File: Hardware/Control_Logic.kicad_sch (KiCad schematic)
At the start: 19 parts, among them IC18 74HC139, IC25 74HC138, IC27 74HC32, IC28 74HC00, IC29 74AHC04, IC30 74HC02, IC31 74HC273, IC32 74HC138, IC49 74HC367, J101 CS Test Points, J7 Decoder

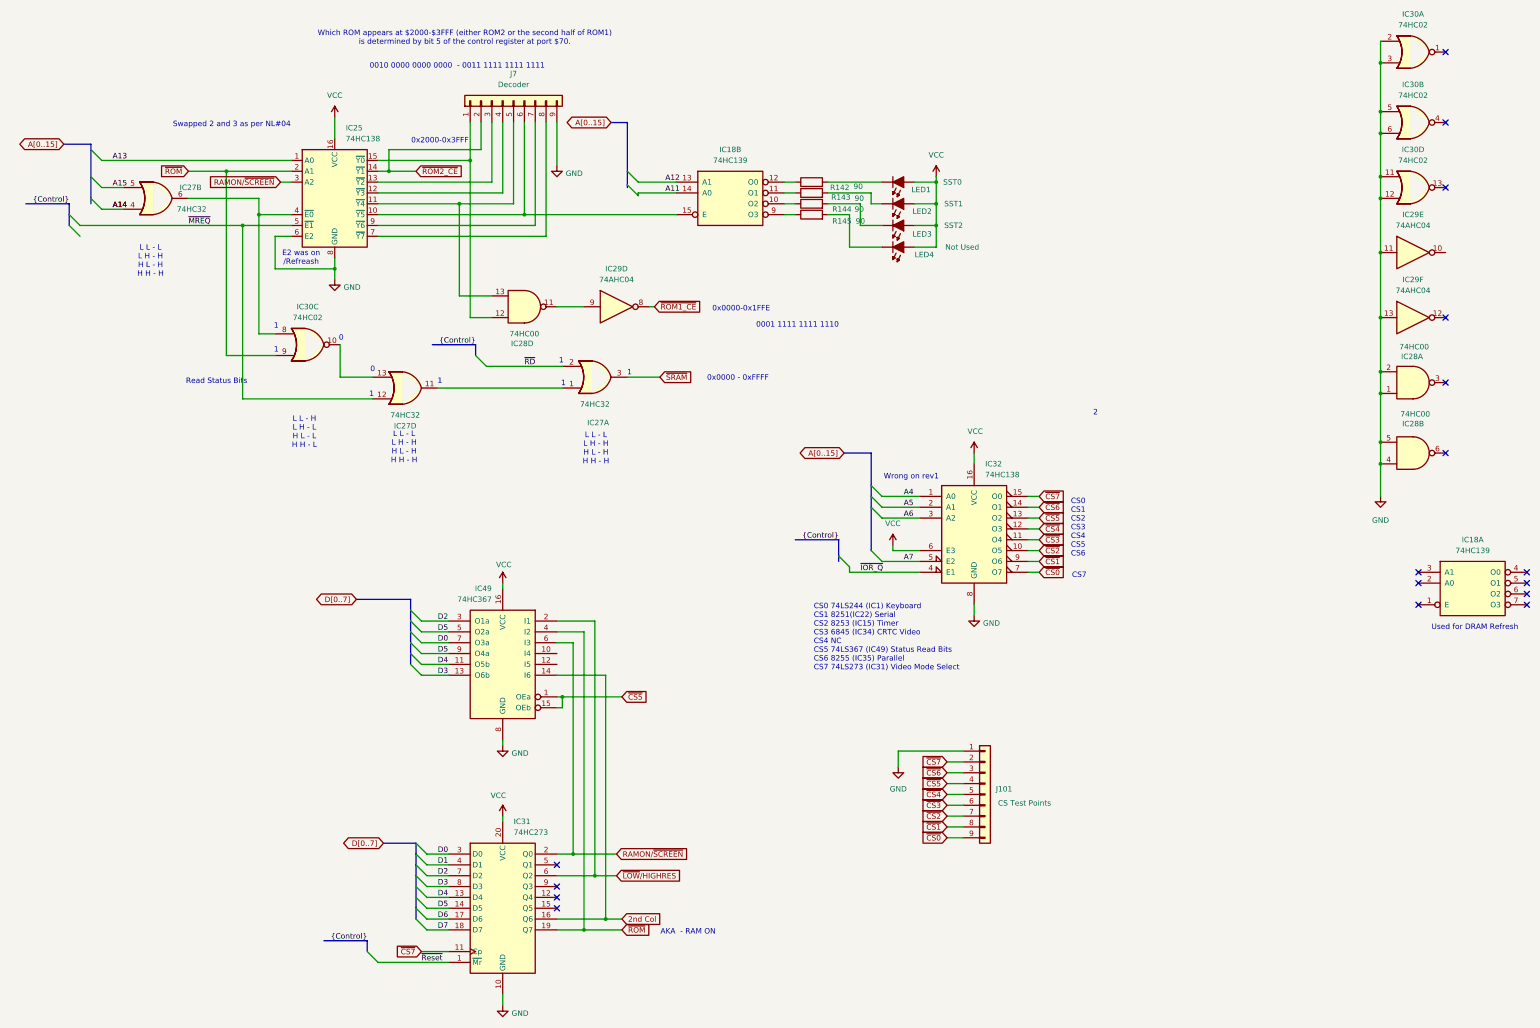
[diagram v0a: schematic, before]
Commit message: Fixed some issues with memory mapping IC 25
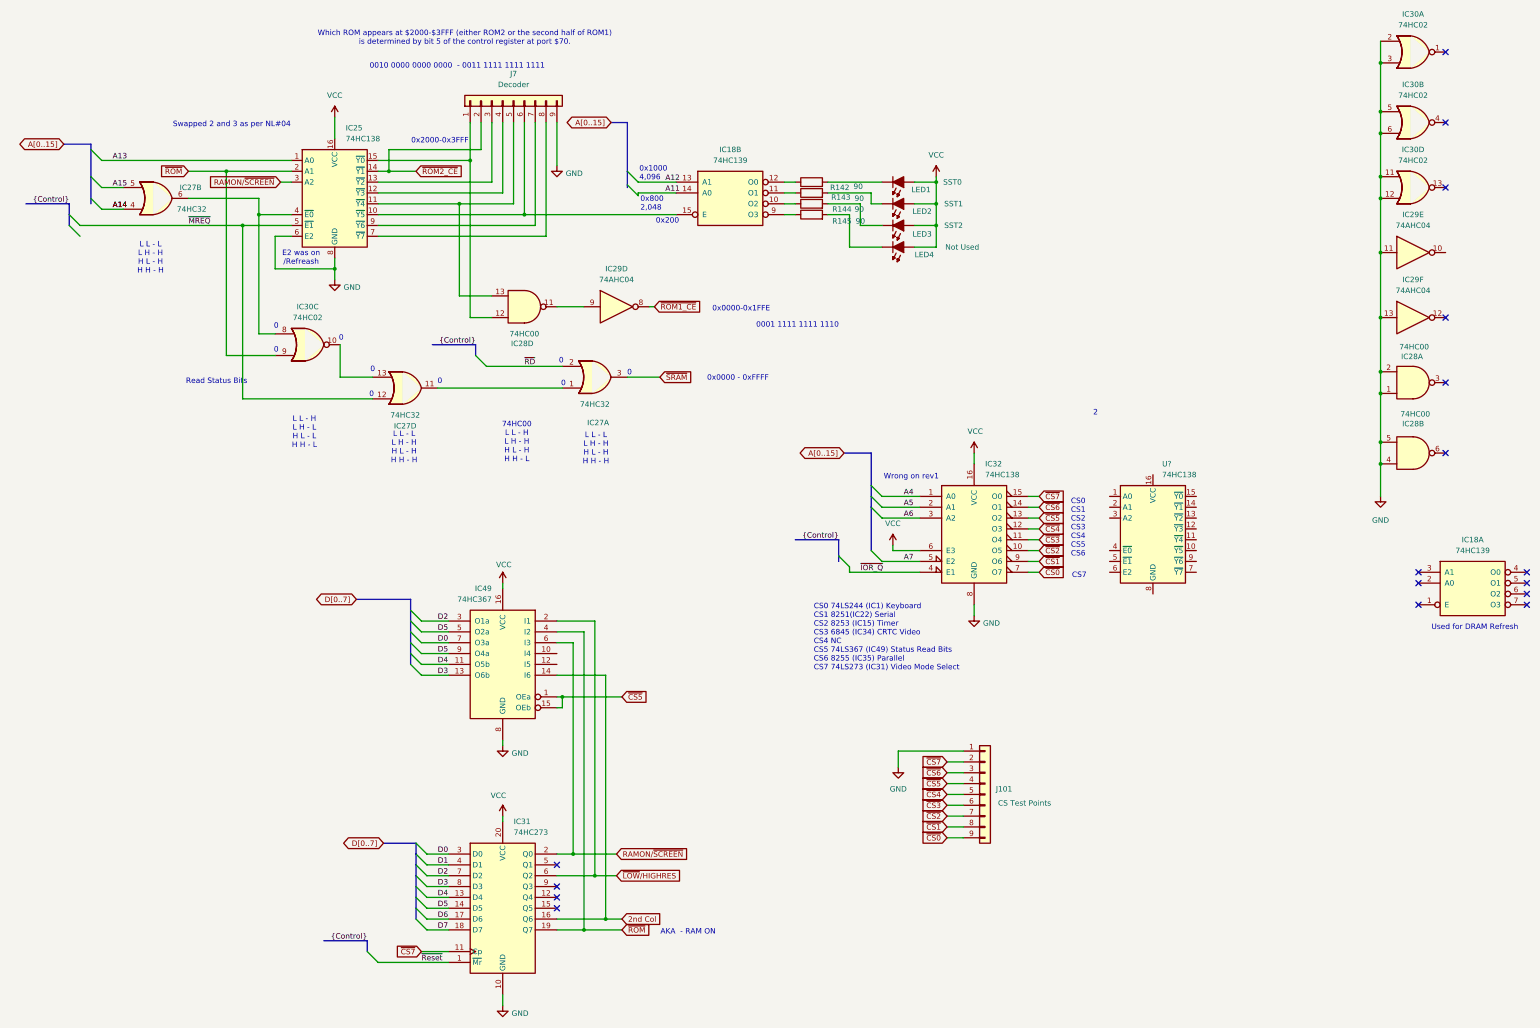
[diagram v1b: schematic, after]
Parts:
- added U?: 74HC138, Package_DIP:DIP-16_W7.62mm_Socket_LongPads, symbol 74xx:74HC138
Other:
- note added: "0x1000 4,096"
- note added: "0x200"
- note added: "0x800 2,048"
- note added: "74HC00 L L - H L H - H H L - H H H - L"
- note removed: "1"
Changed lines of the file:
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@@
 		)
 	)
-	(text "1"
+	(text "0"
 		(exclude_from_sim no)
 		(at 135.128 106.426 0)
@@
 		)
 	)
-	(text "1"
+	(text "0"
 		(exclude_from_sim no)
 		(at 119.126 109.474 0)
@@
 	(text "L L - L\nL H - H\nH L - H\nH H - H"
 		(exclude_from_sim no)
-		(at 67.31 78.232 0)
+		(at 67.31 77.47 0)
 		(effects
 			(font
@@
 		)
 	)
+	(text "0x1000\n4,096"
+		(exclude_from_sim no)
+		(at 181.864 57.658 0)
+		(effects
+			(font
+				(size 1.27 1.27)
+			)
+			(justify left)
+		)
+	)
 	(text "Used for DRAM Refresh"
 		(exclude_from_sim no)
@@
 		)
 	)
+	(text "0x200"
+		(exclude_from_sim no)
+		(at 188.468 68.834 0)
+		(effects
+			(font
+				(size 1.27 1.27)
+			)
+		)
+	)
 	(text "E2 was on \n/Refreash"
 		(exclude_from_sim no)
@@
 		)
 	)
+	(text "0x800 \n2,048"
+		(exclude_from_sim no)
+		(at 182.118 64.77 0)
+		(effects
+			(font
+				(size 1.27 1.27)
+			)
+			(justify left)
+		)
+	)
 	(text "CS0 74LS244 (IC1) Keyboard\nCS1 8251(IC22) Serial\nCS2 8253 (IC15) Timer\nCS3 6845 (IC34) CRTC Video\nCS4 NC\nCS5 74LS367 (IC49) Status Read Bits\nCS6 8255 (IC35) Parallel \nCS7 74LS273 (IC31) Video Mode Select"
 		(exclude_from_sim no)
@@
 		)
 	)
-	(text "1"
+	(text "0"
 		(exclude_from_sim no)
 		(at 164.084 106.934 0)
@@
 		)
 	)
-	(text "1"
+	(text "0"
 		(exclude_from_sim no)
 		(at 163.576 101.6 0)
@@
 		)
 	)
-	(text "1"
+	(text "0"
 		(exclude_from_sim no)
 		(at 179.578 104.394 0)
@@
 		)
 	)
-	(text "1"
+	(text "0"
 		(exclude_from_sim no)
 		(at 96.774 93.472 0)
@@
 		)
 	)
-	(text "1"
+	(text "0"
 		(exclude_from_sim no)
 		(at 96.774 99.06 0)
@@
 		)
 	)
+	(text "74HC00\nL L - H\nL H - H\nH L - H\nH H - L"
+		(exclude_from_sim no)
+		(at 153.162 120.65 0)
+		(effects
+			(font
+				(size 1.27 1.27)
+			)
+		)
+	)
 	(text "0x2000-0x3FFF"
 		(exclude_from_sim no)
@@
 	)
 	(junction
-		(at 88.9 69.85)
+		(at 355.6 63.5)
 		(diameter 0)
 		(color 0 0 0 0)
 	)
 	(junction
-		(at 355.6 63.5)
+		(at 355.6 104.14)
 		(diameter 0)
 		(color 0 0 0 0)
 	)
 	(junction
-		(at 355.6 104.14)
+		(at 139.7 64.77)
 		(diameter 0)
 		(color 0 0 0 0)
 	)
 	(junction
-		(at 139.7 64.77)
+		(at 88.9 69.85)
 		(diameter 0)
 		(color 0 0 0 0)
@@
 	)
 	(bus_entry
+		(at 48.26 67.31)
+		(size 2.54 2.54)
+		(stroke
+			(width 0)
+			(type default)
+		)
+	)
+	(bus_entry
 		(at 53.34 52.07)
 		(size 2.54 2.54)
@@
 	)
 	(bus_entry
-		(at 48.26 67.31)
-		(size 2.54 2.54)
-		(stroke
-			(width 0)
-			(type default)
-		)
-	)
-	(bus_entry
 		(at 128.27 167.64)
 		(size 2.54 2.54)
@@
 	(bus
 		(pts
-			(xy 48.26 67.31) (xy 48.26 69.85)
+			(xy 48.26 64.77) (xy 48.26 67.31)
 		)
 		(stroke
@@
 		)
 	)
+	(bus
+		(pts
+			(xy 48.26 67.31) (xy 48.26 69.85)
+		)
+		(stroke
+			(width 0)
+			(type default)
+		)
+	)
 	(wire
 		(pts
@@
 	(wire
 		(pts
-			(xy 50.8 69.85) (xy 88.9 69.85)
-		)
-		(stroke
-			(width 0)
-			(type default)
-		)
-	)
-	(wire
-		(pts
 			(xy 273.05 133.35) (xy 275.59 133.35)
 		)
@@
 	(bus
 		(pts
-			(xy 48.26 64.77) (xy 48.26 67.31)
-		)
-		(stroke
-			(width 0)
-			(type default)
-		)
-	)
-	(bus
-		(pts
 			(xy 129.54 229.87) (xy 129.54 227.33)
 		)
@@
 	(wire
 		(pts
+			(xy 50.8 69.85) (xy 88.9 69.85)
+		)
+		(stroke
+			(width 0)
+			(type default)
+		)
+	)
+	(wire
+		(pts
 			(xy 171.45 162.56) (xy 171.45 222.25)
 		)
@@
 		)
 	)
-	(label "~{MREQ}"
-		(at 76.2 69.85 0)
-		(effects
-			(font
-				(size 1.27 1.27)
-			)
-			(justify left bottom)
-		)
-	)
 	(label "{Control}"
 		(at 118.11 237.49 180)
@@
 		)
 	)
+	(label "~{MREQ}"
+		(at 76.2 69.85 0)
+		(effects
+			(font
+				(size 1.27 1.27)
+			)
+			(justify left bottom)
+		)
+	)
 	(label "{Control}"
 		(at 48.26 64.77 180)
@@
 					(unit 1)
 				)
+			)
+		)
+	)
+	(symbol
+		(lib_id "74xx:74HC138")
+		(at 302.26 143.51 0)
+		(unit 1)
+		(exclude_from_sim no)
+		(in_bom yes)
+		(on_board yes)
+		(dnp no)
+		(fields_autoplaced yes)
+		(property "Reference" "U?"
+			(at 304.4033 125.73 0)
+			(effects
+				(font
+					(size 1.27 1.27)
+				)
+				(justify left)
+			)
+		)
+		(property "Value" "74HC138"
+			(at 304.4033 128.27 0)
+			(effects
+				(font
+					(size 1.27 1.27)
+				)
+				(justify left)
+			)
+		)
+		(property "Footprint" "Package_DIP:DIP-16_W7.62mm_Socket_LongPads"
+			(at 302.26 143.51 0)
+			(effects
+				(font
+					(size 1.27 1.27)
+				)
+				(hide yes)
+			)
+		)
+		(property "Datasheet" "http://www.ti.com/lit/ds/symlink/cd74hc238.pdf"
+			(at 302.26 143.51 0)
+			(effects
+				(font
+					(size 1.27 1.27)
+				)
+				(hide yes)
+			)
+		)
+		(property "Description" "3-to-8 line decoder/multiplexer inverting, DIP-16/SOIC-16/SSOP-16"
+			(at 302.26 143.51 0)
+			(effects
+				(font
+					(size 1.27 1.27)
+				)
+				(hide yes)
+			)
+		)
+		(pin "5"
+		)
+		(pin "3"
+		)
+		(pin "16"
+		)
+		(pin "12"
+		)
+		(pin "10"
+		)
+		(pin "7"
+		)
+		(pin "13"
+		)
+		(pin "15"
+		)
+		(pin "1"
+		)
+		(pin "2"
+		)
+		(pin "4"
+		)
+		(pin "8"
+		)
+		(pin "6"
+		)
+		(pin "14"
+		)
+		(pin "11"
+		)
+		(pin "9"
+		)
+		(instances
+			(project ""
+				(path "/f5b991b2-bbcb-4d6c-a89c-6801c3d50251/e785100f-5c94-459c-92b4-9599172952bf"
+					(reference "U?")
+					(unit 1)
+				)
